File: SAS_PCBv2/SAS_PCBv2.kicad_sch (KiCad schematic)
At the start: 1 part, among them J2 GPIO_CONNECTOR

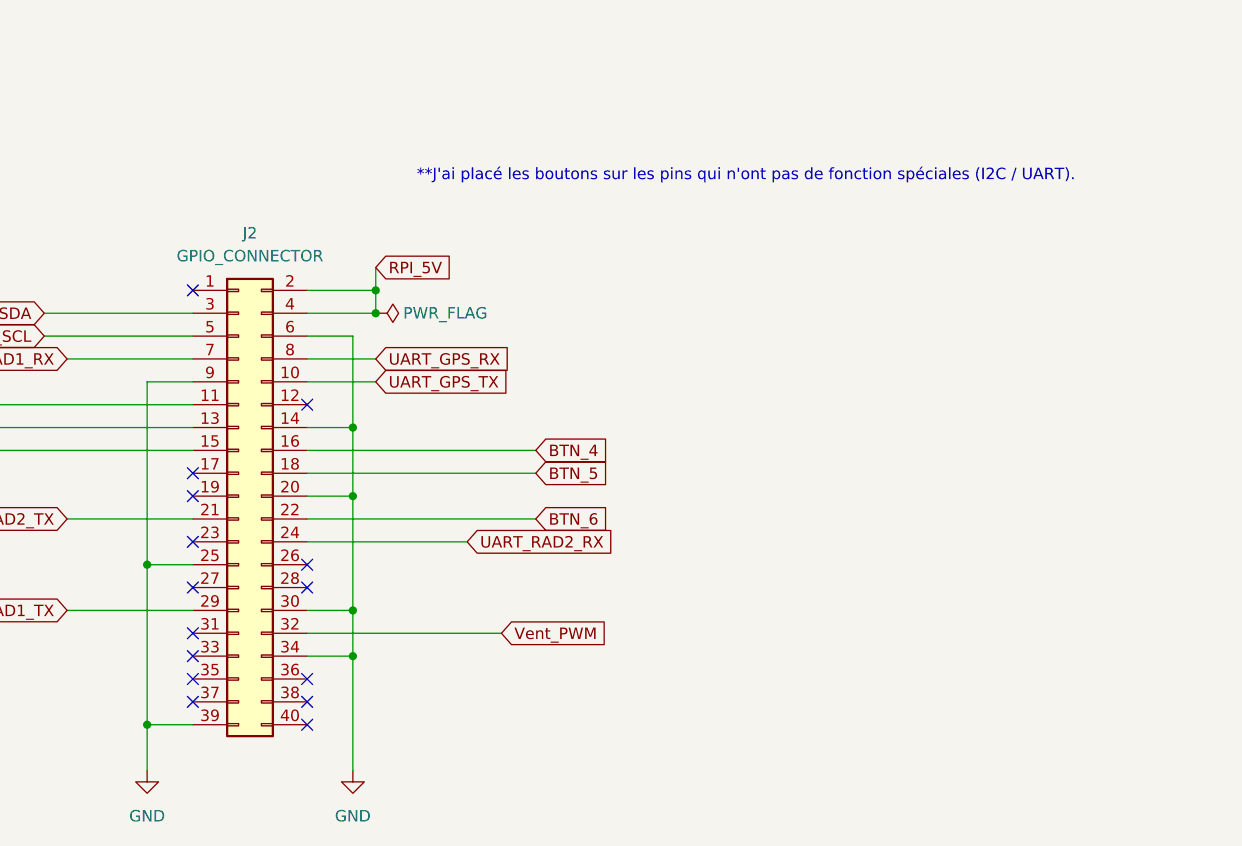
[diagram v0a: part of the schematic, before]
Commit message: Amélioration des modèles Rpi et page power, switch PCB/USB fonctionnelle
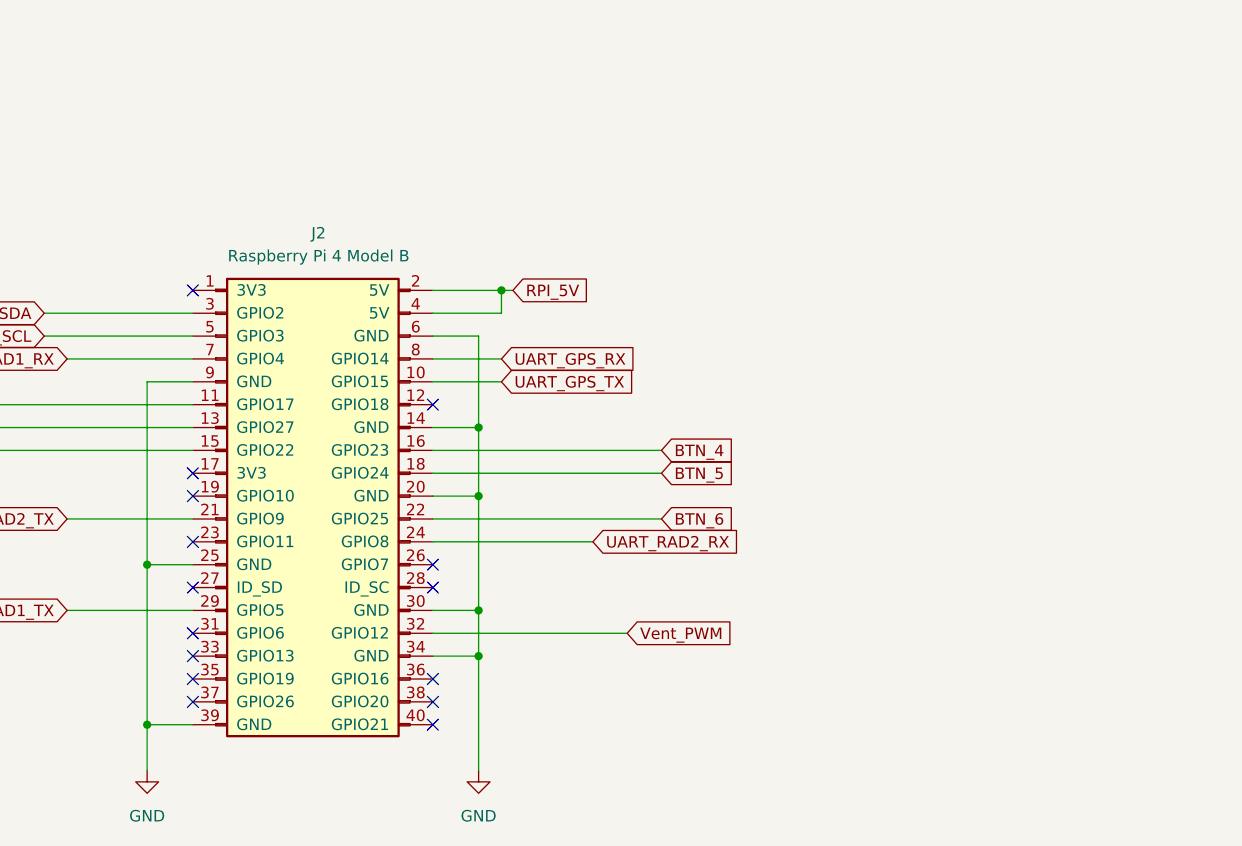
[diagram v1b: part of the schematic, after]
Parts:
- J2: value GPIO_CONNECTOR -> Raspberry Pi 4 Model B
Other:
- note removed: "**J'ai placé les boutons sur les pins qui n'ont pas de fonction spéciales (I2C / UART)."

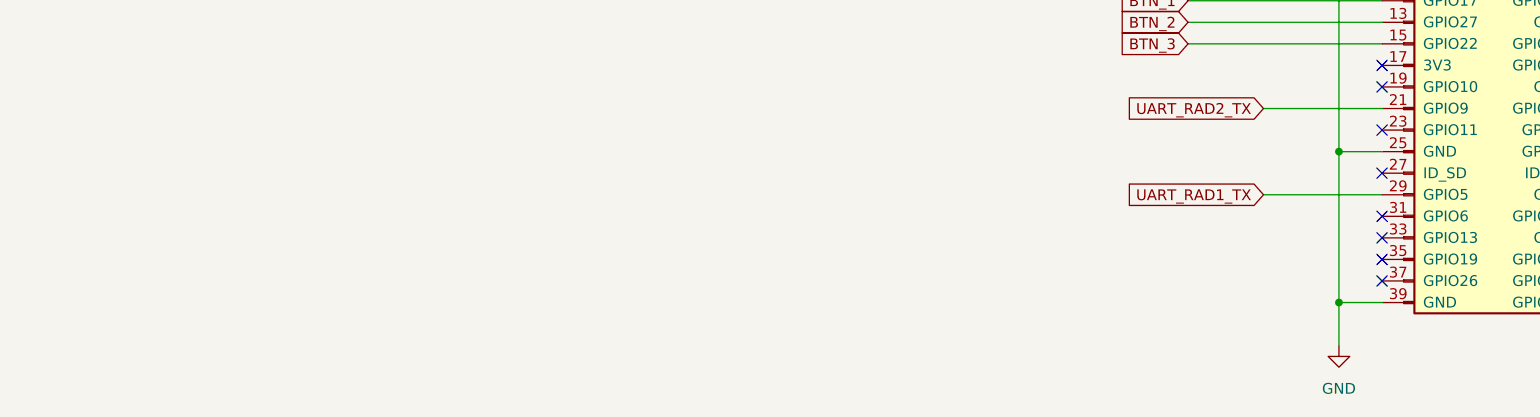
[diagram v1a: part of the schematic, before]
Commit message: Identification des transistors, footprint BMP280 et GPS Neo-6M, correction du fan PWM
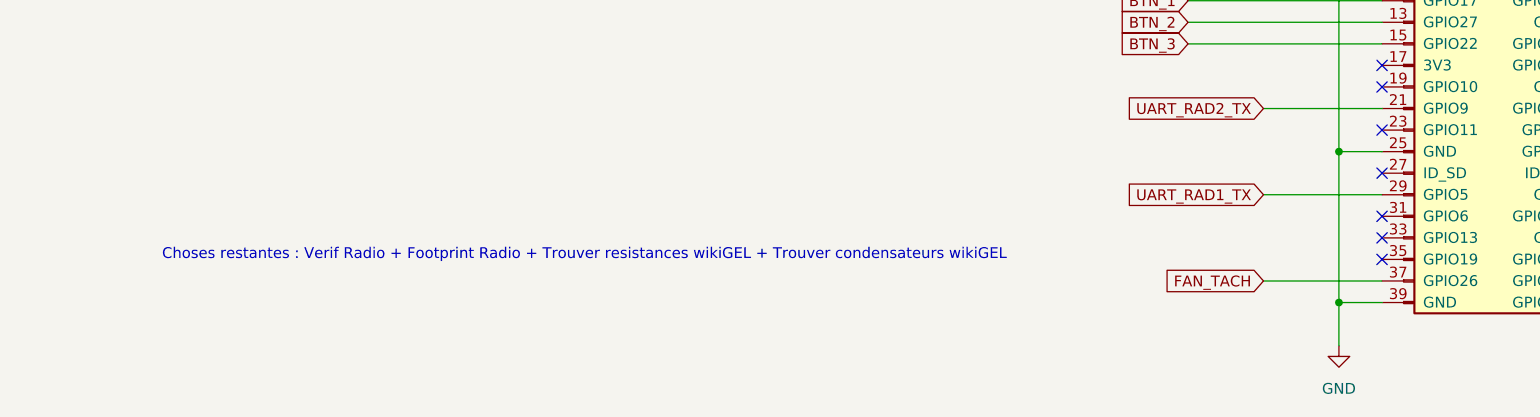
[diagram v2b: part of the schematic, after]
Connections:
- net FAN_TACH: now reaches J2.37 (GPIO26)
- no-connect marks 15 -> 14
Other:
- note added: "Choses restantes : Verif Radio + Footprint Radio + Trouver resistances wikiGEL + Trouver condensateurs wikiGEL"
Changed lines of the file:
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@@
 	(generator_version "9.0")
 	(paper "A4")
+	(text "Choses restantes : Verif Radio + Footprint Radio + Trouver resistances wikiGEL + Trouver condensateurs wikiGEL"
+		(exclude_from_sim no)
+		(at 72.39 123.952 0)
+		(effects
+			(font
+				(size 1.27 1.27)
+			)
+		)
+	)
 	(junction
 		(at 198.12 96.52)
@@
 		(at 166.37 121.92)
 	)
-	(no_connect
-		(at 166.37 127)
-	)
 	(wire
 		(pts
@@
 	(wire
 		(pts
+			(xy 152.4 127) (xy 166.37 127)
+		)
+		(stroke
+			(width 0)
+			(type default)
+		)
+	)
+	(wire
+		(pts
 			(xy 201.93 81.28) (xy 200.66 81.28)
 		)
@@
 				(hide yes)
 			)
+		)
+	)
+	(global_label "FAN_TACH"
+		(shape input)
+		(at 152.4 127 180)
+		(fields_autoplaced yes)
+		(effects
+			(font
+				(size 1.27 1.27)
+			)
+			(justify right)
+		)
+		(property "Intersheetrefs" "${INTERSHEET_REFS}"
+			(at 135.0819 127 0)
+			(effects
+				(font
+					(size 1.27 1.27)
+				)
+				(justify right)
+				(hide yes)
+			)

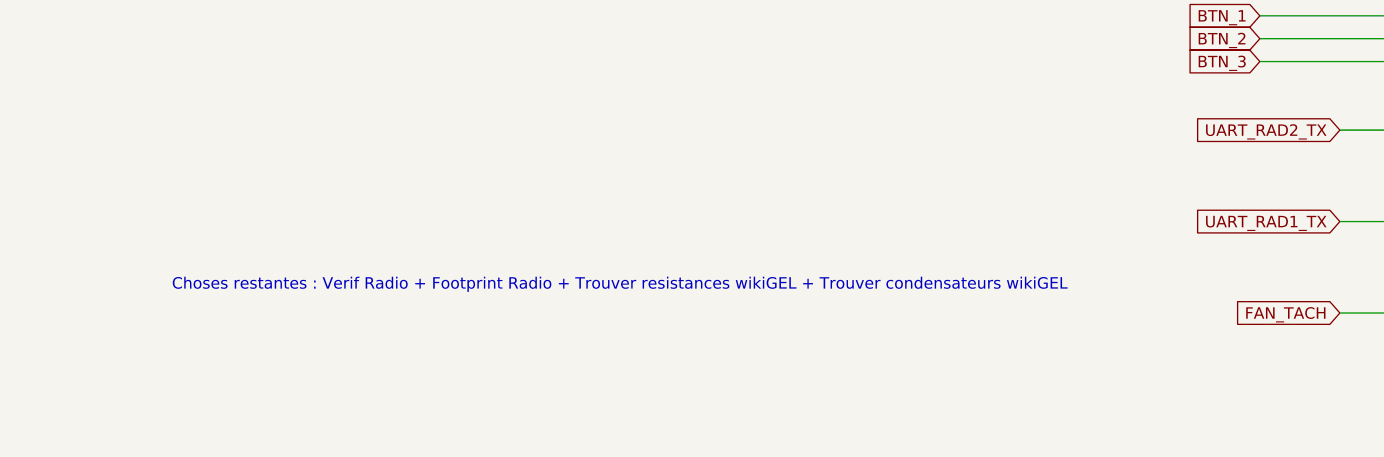
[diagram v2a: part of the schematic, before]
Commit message: Ajout du connecteur spécial pour les radios, insertion des footprints dans le PCB, fin du schéma
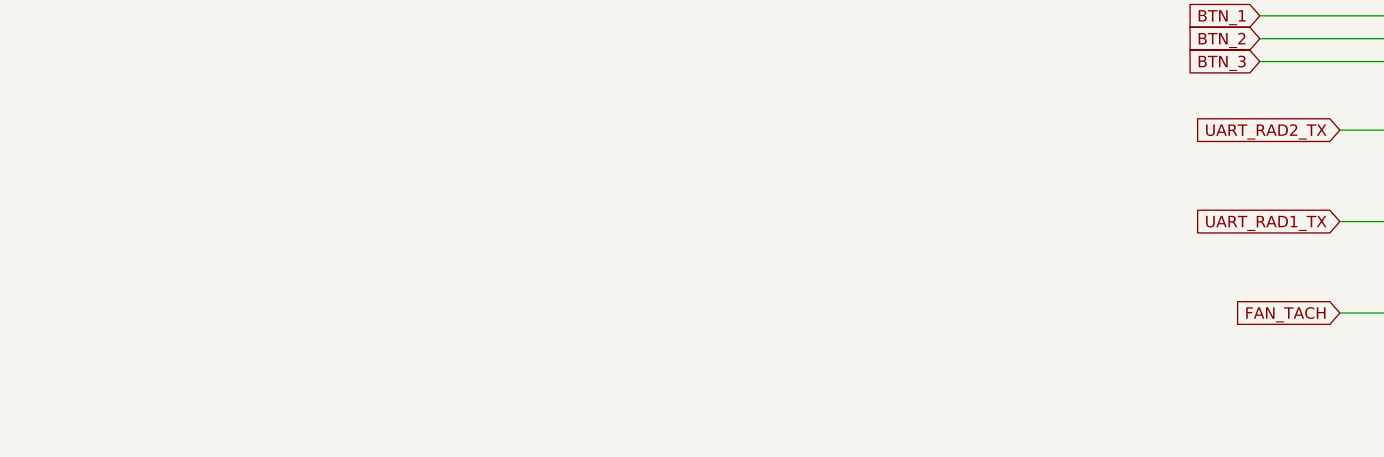
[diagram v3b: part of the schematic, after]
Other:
- note removed: "Choses restantes : Verif Radio + Footprint Radio + Trouver resistances wikiGEL + Trouver condensateurs wikiGEL"
